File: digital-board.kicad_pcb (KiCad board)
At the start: 2 copper layers, 200 x 150 mm, 241 parts, among them IC1 ATMEGA6450-A, J1 CONN_20X2, Q1 2N3904, Q2 2N3904, SW15 TACT_SWITCH, SW16 TACT_SWITCH, SW17 TACT_SWITCH, SW18 TACT_SWITCH, SW19 TACT_SWITCH, SW20 TACT_SWITCH, SW21 TACT_SWITCH, SW22 TACT_SWITCH, SW23 TACT_SWITCH, U1 DG419, U10 74LVC1G32, U11 74HC165, U12 74AC595, U13 74AC595, U14 74HC165, U15 74AC595, U16 74AC595, U2 74HC4067, U3 R-78E5.0-1.0, U4 74HC4067, U5 74LS573, U6 74LS573, U7 74LVC2G04, U8 74AC595, U9 74HC165, X1 MIDI OUT, X2 MIDI IN, X3 MIDI THRU

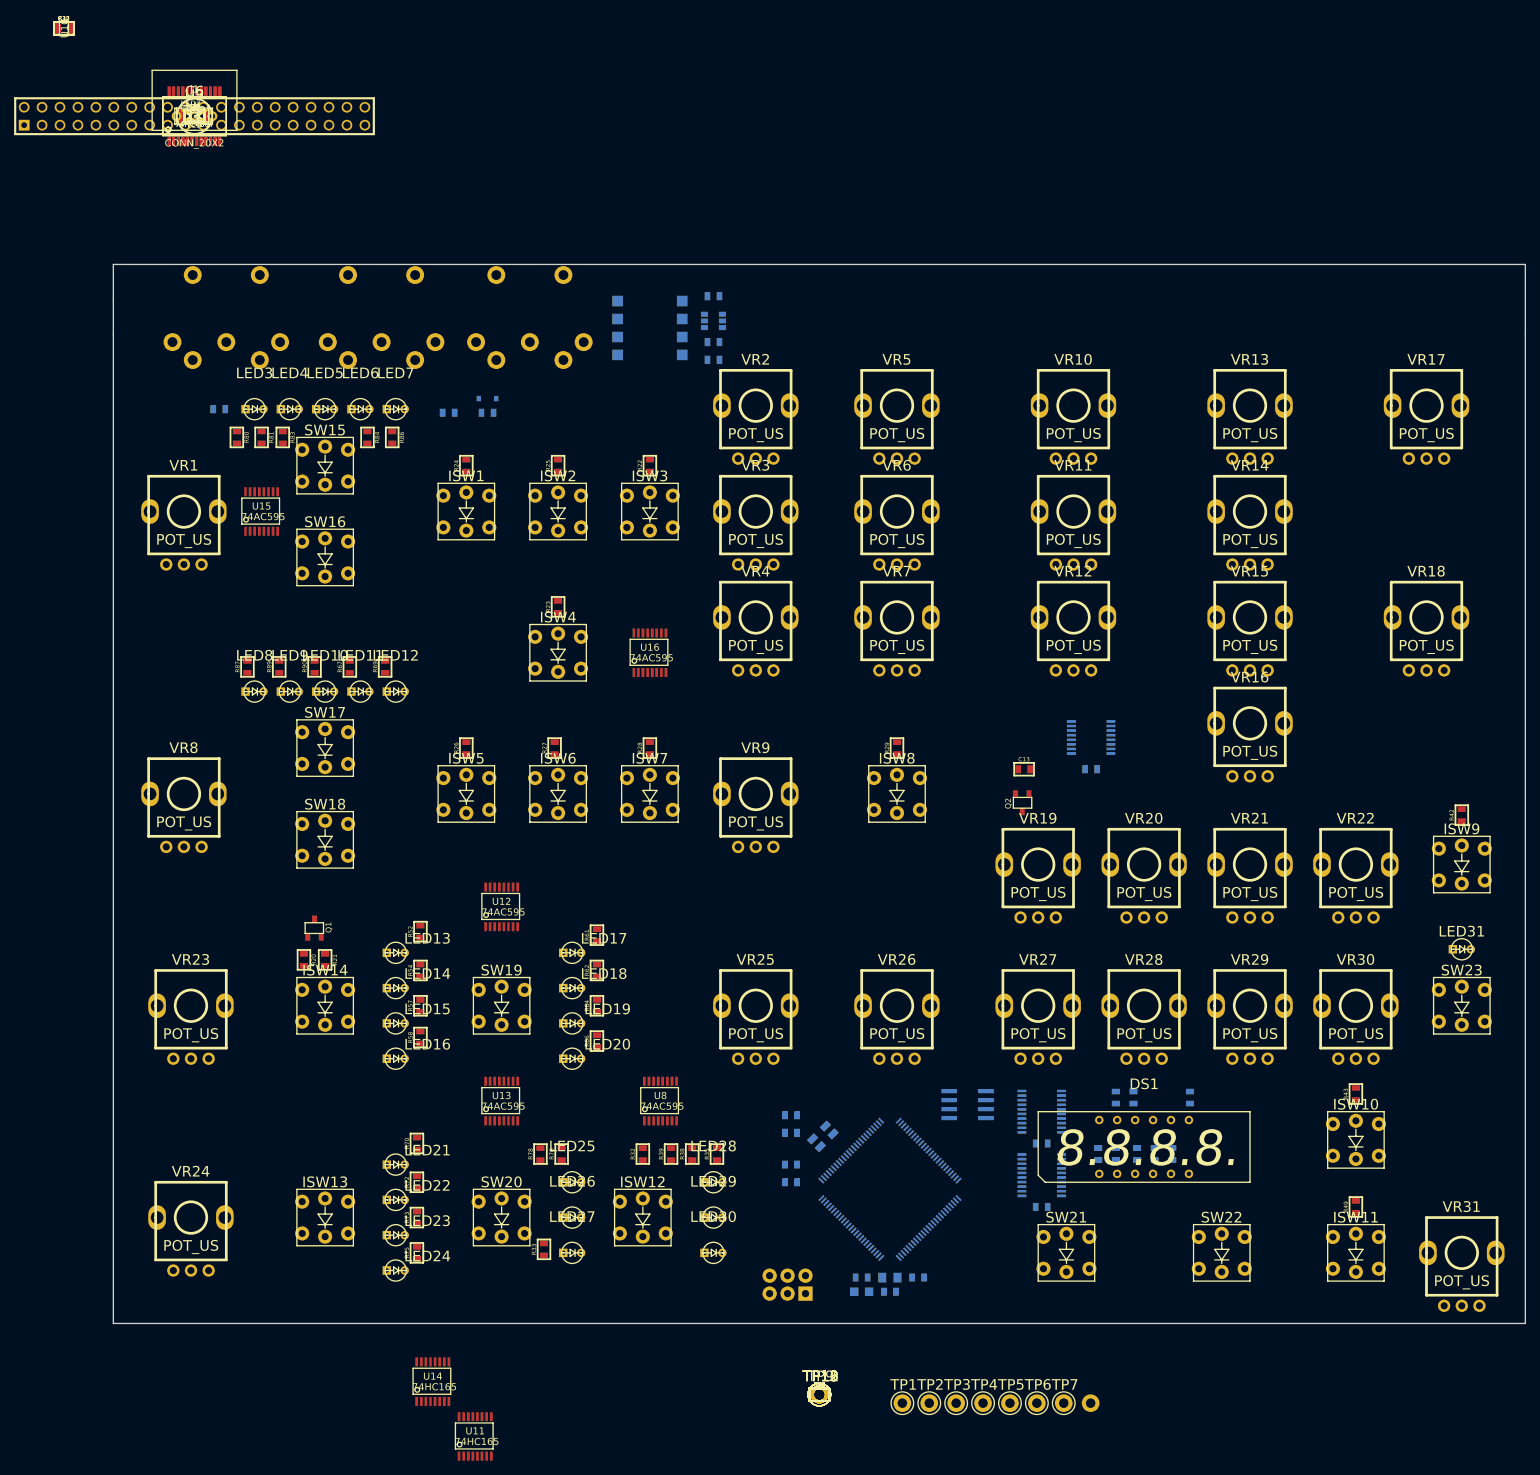
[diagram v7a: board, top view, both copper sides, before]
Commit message: layout of switch interface
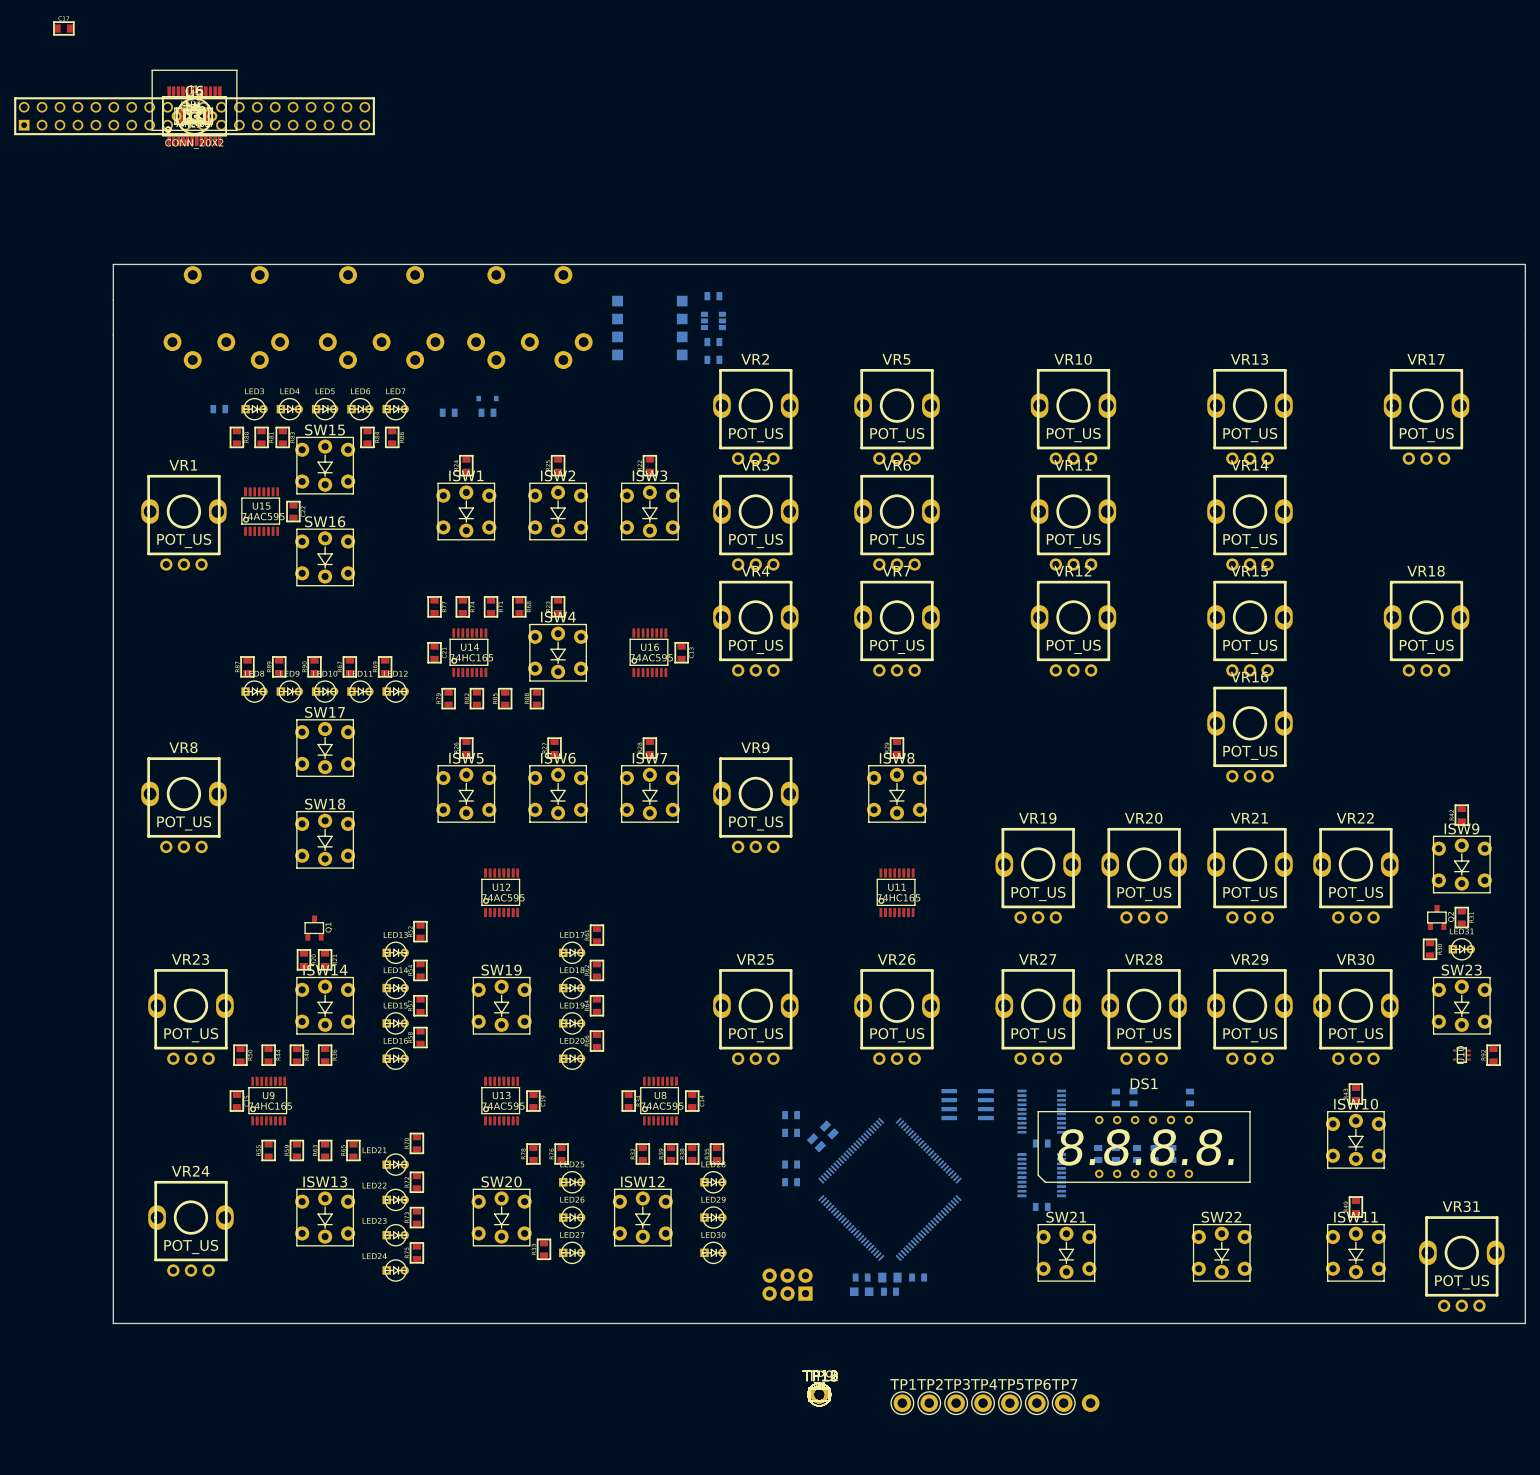
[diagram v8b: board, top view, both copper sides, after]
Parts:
- C14, U9: moved to F.Cu
- moved U10 245.7 mm to (191.0, 112.0), turned to 180 degrees
- moved R31 234.7 mm to (191.0, 92.5), turned to 270 degrees
- moved R30 233.4 mm to (186.5, 97.0), turned to 270 degrees
- moved C22 145.6 mm to (25.5, 35.0), turned to 270 degrees
- moved C15 139.6 mm to (17.5, 118.5), turned to 270 degrees
- moved U9 127.4 mm to (22.0, 118.5), turned to 0 degrees
- moved R77 124.2 mm to (45.5, 48.5), turned to 270 degrees
- moved R74 122.5 mm to (49.5, 48.5), turned to 270 degrees
- moved R71 120.9 mm to (53.5, 48.5), turned to 270 degrees
- moved R68 119.4 mm to (57.5, 48.5), turned to 270 degrees
- moved C21 118.4 mm to (45.5, 55.0), turned to 270 degrees
- moved R79 111.7 mm to (47.5, 61.5), turned to 90 degrees
- moved R82 109.9 mm to (51.5, 61.5), turned to 90 degrees
- moved R85 108.2 mm to (55.5, 61.5), turned to 90 degrees
- moved R92 106.9 mm to (195.5, 112.0), turned to 90 degrees
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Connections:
- R36 pad 2: Net-(R36-Pad2) -> Net-(ISW14-Pad3)
- R37 pad 2: Net-(ISW8-Pad3) -> Net-(ISW9-Pad3)
- R41 pad 2: Net-(ISW9-Pad3) -> Net-(ISW8-Pad3)
- R45 pad 2: Net-(ISW10-Pad3) -> Net-(R45-Pad2)
- R51 pad 2: Net-(ISW11-Pad3) -> Net-(R51-Pad2)
- R55 pad 2: Net-(ISW14-Pad3) -> Net-(ISW13-Pad3)
- R56 pad 2: Net-(R56-Pad2) -> Net-(ISW11-Pad3)
- R59 pad 2: Net-(ISW13-Pad3) -> Net-(R59-Pad2)
- R60 pad 2: Net-(R60-Pad2) -> Net-(ISW10-Pad3)
- R63 pad 2: Net-(R63-Pad2) -> Net-(ISW12-Pad3)
- R65 pad 2: Net-(ISW12-Pad3) -> Net-(R65-Pad2)
- R68 pad 2: Net-(ISW1-Pad3) -> Net-(ISW3-Pad3)
- R74 pad 2: Net-(ISW3-Pad3) -> Net-(ISW1-Pad3)
- R77 pad 2: Net-(ISW4-Pad3) -> Net-(R77-Pad2)
- R88 pad 2: Net-(R88-Pad2) -> Net-(ISW4-Pad3)
- SW15 pad 3: Net-(R88-Pad2) -> Net-(R77-Pad2)
- SW15 pad 4: Net-(R88-Pad2) -> Net-(R77-Pad2)
- SW16 pad 3: Net-(R36-Pad2) -> Net-(R50-Pad2)
- SW16 pad 4: Net-(R36-Pad2) -> Net-(R50-Pad2)
- SW17 pad 3: Net-(R40-Pad2) -> Net-(R44-Pad2)
- SW17 pad 4: Net-(R40-Pad2) -> Net-(R44-Pad2)
- SW18 pad 3: Net-(R44-Pad2) -> Net-(R40-Pad2)
- SW18 pad 4: Net-(R44-Pad2) -> Net-(R40-Pad2)
- SW19 pad 3: Net-(R50-Pad2) -> Net-(R65-Pad2)
- SW19 pad 4: Net-(R50-Pad2) -> Net-(R65-Pad2)
- SW20 pad 3: Net-(R63-Pad2) -> Net-(R59-Pad2)
- SW20 pad 4: Net-(R63-Pad2) -> Net-(R59-Pad2)
- SW21 pad 3: Net-(R56-Pad2) -> Net-(R45-Pad2)
- SW21 pad 4: Net-(R56-Pad2) -> Net-(R45-Pad2)
- SW22 pad 3: Net-(R60-Pad2) -> Net-(R51-Pad2)
- SW22 pad 4: Net-(R60-Pad2) -> Net-(R51-Pad2)
- U11 pad 11: Net-(ISW8-Pad3) -> GND
- U11 pad 12: Net-(ISW9-Pad3) -> GND
- U11 pad 13: Net-(ISW10-Pad3) -> Net-(ISW9-Pad3)
- U11 pad 14: Net-(ISW11-Pad3) -> Net-(ISW8-Pad3)
- U11 pad 3: Net-(R56-Pad2) -> Net-(R45-Pad2)
- U11 pad 4: Net-(R60-Pad2) -> Net-(R51-Pad2)
- U11 pad 5: GND -> Net-(ISW11-Pad3)
- U11 pad 6: GND -> Net-(ISW10-Pad3)
- U14 pad 11: Net-(ISW1-Pad3) -> Net-(ISW3-Pad3)
- U14 pad 13: Net-(ISW3-Pad3) -> Net-(ISW1-Pad3)
- U14 pad 14: Net-(ISW4-Pad3) -> Net-(R77-Pad2)
- U14 pad 6: Net-(R88-Pad2) -> Net-(ISW4-Pad3)
- U9 pad 11: Net-(R36-Pad2) -> Net-(ISW14-Pad3)
- U9 pad 3: Net-(ISW14-Pad3) -> Net-(ISW13-Pad3)
- U9 pad 4: Net-(ISW13-Pad3) -> Net-(R59-Pad2)
- U9 pad 5: Net-(R63-Pad2) -> Net-(ISW12-Pad3)
- U9 pad 6: Net-(ISW12-Pad3) -> Net-(R65-Pad2)
